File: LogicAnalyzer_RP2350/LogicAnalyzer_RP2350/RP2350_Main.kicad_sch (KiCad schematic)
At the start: 37 parts, among them J3 SM03B-SRSS-TB, SW1 SW_MEC_5G, SW2 SW_MEC_5G, U3 RP2350A, U4 W25Q128JVS, Y1 12Mhz

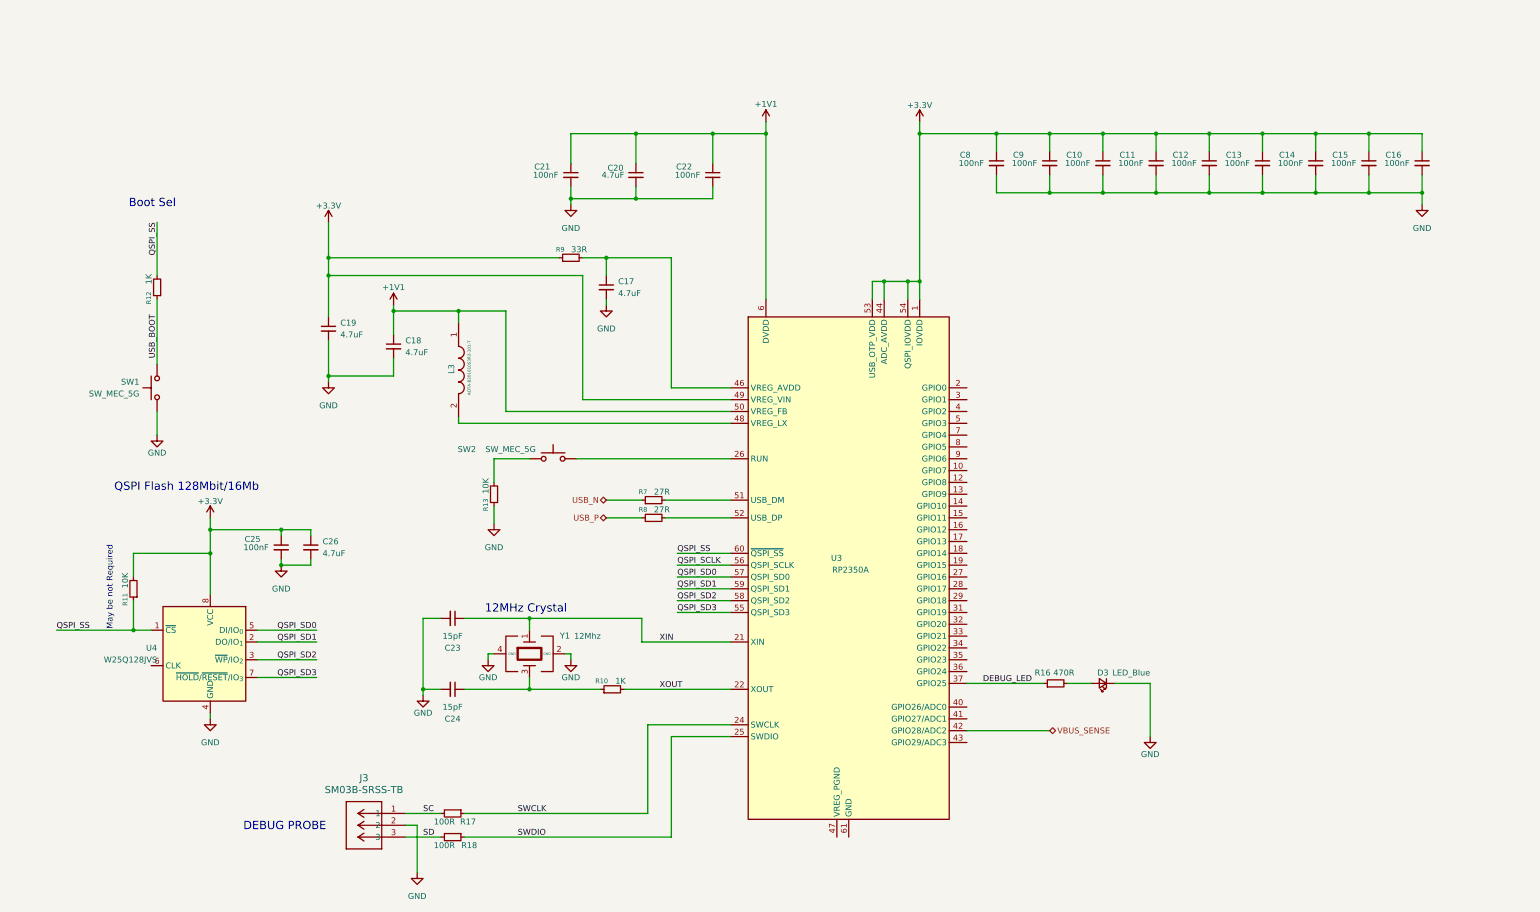
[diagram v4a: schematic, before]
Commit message: Added Buses for Logic Input Pins and Sheet for Shift Registers
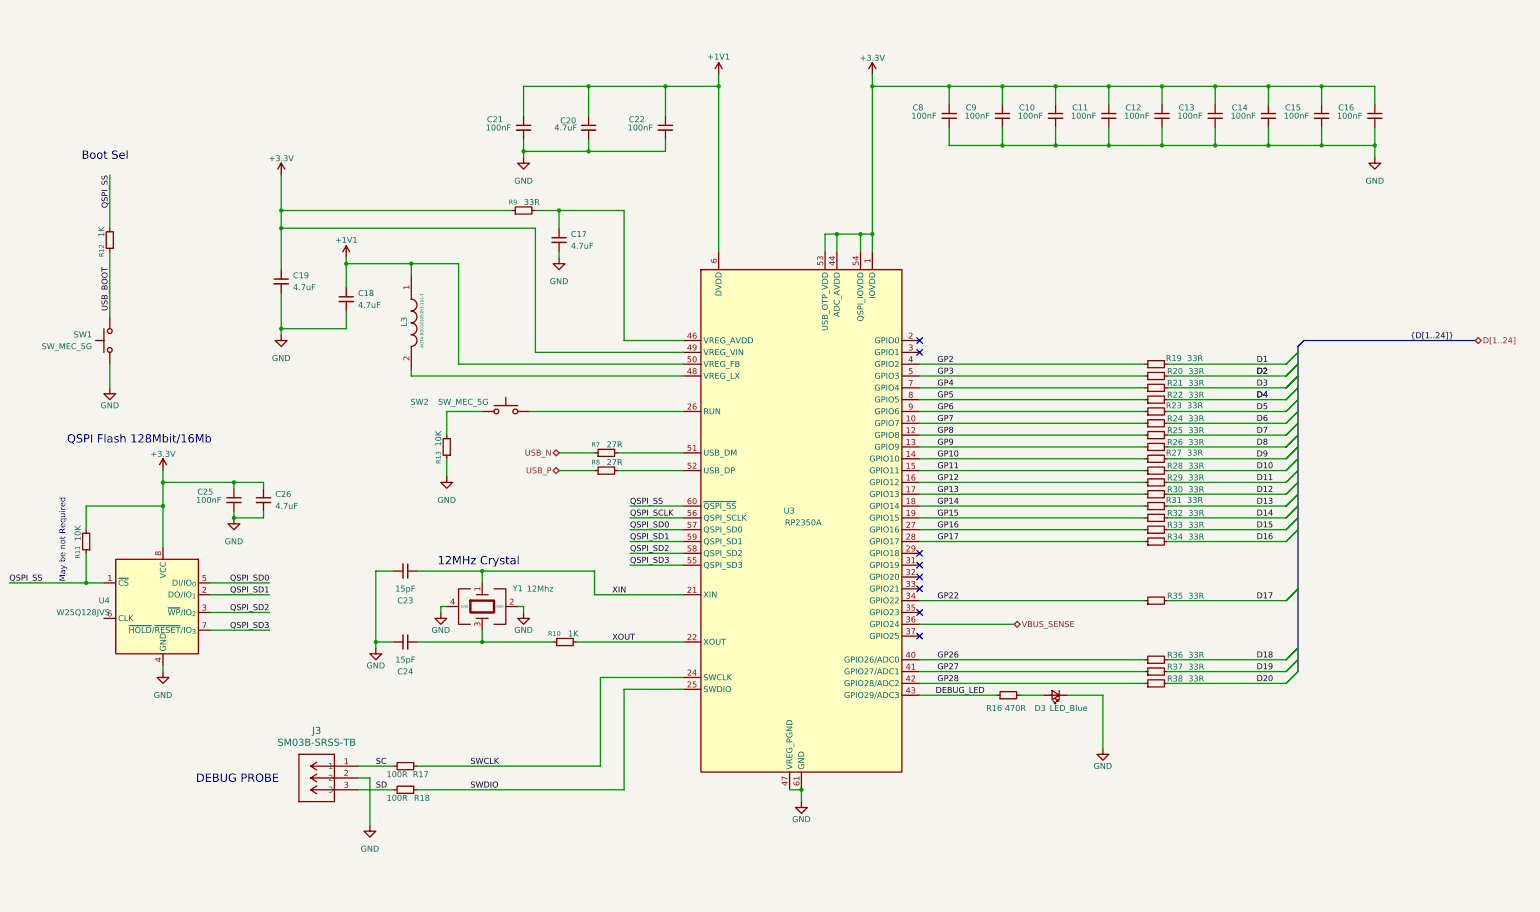
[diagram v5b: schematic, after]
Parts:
- added R19, R20, R21, R22, R23, R24, R25, R26, R27, R28, R29, R30, R31, R32, R33, R34, R35, R36, R37, R38: 33R, Resistor_SMD:R_0603_1608Metric_Pad0.98x0.95mm_HandSolder, symbol Device:R_Small
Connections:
- net DEBUG_LED: now also U3.43 (GPIO29/ADC3); no longer U3.37 (GPIO25)
- net GND: now also U3.47 (VREG_PGND), U3.61 (GND)
- net VBUS_SENSE: now also U3.36 (GPIO24); no longer U3.42 (GPIO28/ADC2)
- net GP7: now reaches U3.10 (GPIO7)
- net GP7: now also R24.1
- net GP8: now reaches U3.12 (GPIO8)
- net GP8: now also R25.1
- net GP9: now reaches U3.13 (GPIO9)
- net GP9: now also R26.1
- net GP10: now reaches U3.14 (GPIO10)
- net GP10: now also R27.1
- net GP11: now reaches U3.15 (GPIO11)
- net GP11: now also R28.1
- net GP12: now reaches U3.16 (GPIO12)
- net GP12: now also R29.1
- net GP13: now reaches U3.17 (GPIO13)
- net GP13: now also R30.1
- net GP14: now reaches U3.18 (GPIO14)
- net GP14: now also R31.1
- net GP15: now reaches U3.19 (GPIO15)
- net GP15: now also R32.1
- net GP16: now reaches U3.27 (GPIO16)
- net GP16: now also R33.1
- net GP17: now reaches U3.28 (GPIO17)
- net GP17: now also R34.1
- net GP22: now reaches U3.34 (GPIO22)
- net GP22: now also R35.1
- net GP2: now reaches U3.4 (GPIO2)
- net GP2: now also R19.1
- net GP26: now reaches U3.40 (GPIO26/ADC0)
- net GP26: now also R36.1
- net GP27: now reaches U3.41 (GPIO27/ADC1)
- net GP27: now also R37.1
- net GP3: now reaches U3.5 (GPIO3)
- net GP3: now also R20.1
- net GP4: now reaches U3.7 (GPIO4)
- net GP4: now also R21.1
- net GP5: now reaches U3.8 (GPIO5)
- net GP5: now also R22.1
- net GP6: now reaches U3.9 (GPIO6)
- net GP6: now also R23.1
- new net D1: R19.2
- new net D10: R28.2
- new net D11: R29.2
- new net D12: R30.2
- new net D13: R31.2
- new net D14: R32.2
- new net D15: R33.2
- new net D16: R34.2
- new net D17: R35.2
- new net D18: R36.2
- new net D19: R37.2
- new net D2: R20.2
- new net D20: R38.2
- new net D3: R21.2
- new net D4: R22.2
- new net D5: R23.2
- new net D6: R24.2
- new net D7: R25.2
- new net D8: R26.2
- new net D9: R27.2
- new net GP28: R38.1, U3.42 (GPIO28/ADC2)
- no-connect marks 0 -> 8
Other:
- moved on the sheet: C10, C11, C12, C13, C14, C15, C16, C17, C18, C19, C20, C21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

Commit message: Renaming
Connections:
- net DEBUG_LED renamed Debug_Led
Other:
- note added: "DEBUG Led"
- note added: "RESET"
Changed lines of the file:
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@@
+		)
+	)
+	(text "DEBUG Led"
+		(exclude_from_sim no)
+		(at 256.794 191.262 0)
+		(effects
+			(font
+				(size 1.778 1.778)
+				(color 0 0 255 1)
+			)
+		)
+	)
+	(text "RESET"
+		(exclude_from_sim no)
+		(at 118.872 130.556 90)
+		(effects
+			(font
+				(size 1.778 1.778)
+				(color 0 0 255 1)
+			)
 		)
 	)
@@
 		)
 	)
-	(label "DEBUG_LED"
+	(label "Debug_Led"
 		(at 242.57 184.15 180)
 		(effects
 			(font
 				(size 1.27 1.27)
-				(color 0 0 255 1)
+				(color 0 0 0 1)
 			)
 			(justify right bottom)

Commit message: Added EXT VREF, TRIG, ROTARY SWITCH, DAISY CHAIN CONNECTIONS etc
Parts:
- added R41: 33R, Resistor_SMD:R_0603_1608Metric_Pad0.98x0.95mm_HandSolder, symbol Device:R_Small
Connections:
- net at U3.2 (GPIO0): now also U3.3 (GPIO1), R41.1
- new net EXT_CHAIN: R41.2
- no-connect marks 8 -> 6
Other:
- moved on the sheet: R13, SW2
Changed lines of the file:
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@@
 	(text "RESET"
 		(exclude_from_sim no)
-		(at 118.872 130.556 90)
+		(at 107.442 130.556 90)
 		(effects
 			(font
@@
 	)
 	(junction
+		(at 229.87 107.95)
+		(diameter 0)
+		(color 0 0 0 0)
+	)
+	(junction
 		(at 292.1 66.04)
 		(diameter 0)
@@
 	)
 	(no_connect
-		(at 228.6 107.95)
-	)
-	(no_connect
 		(at 228.6 158.75)
 	)
@@
 		(at 228.6 171.45)
 	)
-	(no_connect
-		(at 228.6 110.49)
-	)
 	(bus_entry
 		(at 307.34 113.03)
@@
 	(wire
 		(pts
-			(xy 151.13 132.08) (xy 158.75 132.08)
+			(xy 139.7 132.08) (xy 158.75 132.08)
 		)
 		(stroke
@@
 	(wire
 		(pts
-			(xy 151.13 135.89) (xy 158.75 135.89)
+			(xy 139.7 135.89) (xy 158.75 135.89)
 		)
 		(stroke
@@
 	(wire
 		(pts
-			(xy 144.78 123.19) (xy 177.8 123.19)
+			(xy 133.35 123.19) (xy 177.8 123.19)
 		)
 		(stroke
@@
 	(wire
 		(pts
+			(xy 229.87 107.95) (xy 229.87 110.49)
+		)
+		(stroke
+			(width 0)
+			(type default)
+		)
+	)
+	(wire
+		(pts
 			(xy 228.6 148.59) (xy 276.86 148.59)
 		)
@@
 	(wire
 		(pts
+			(xy 229.87 107.95) (xy 245.11 107.95)
+		)
+		(stroke
+			(width 0)
+			(type default)
+		)
+	)
+	(wire
+		(pts
 			(xy 260.35 184.15) (xy 267.97 184.15)
 		)
@@
 	(wire
 		(pts
+			(xy 228.6 110.49) (xy 229.87 110.49)
+		)
+		(stroke
+			(width 0)
+			(type default)
+		)
+	)
+	(wire
+		(pts
 			(xy 158.75 162.56) (xy 158.75 157.48)
 		)
@@
 	(wire
 		(pts
+			(xy 250.19 107.95) (xy 265.43 107.95)
+		)
+		(stroke
+			(width 0)
+			(type default)
+		)
+	)
+	(wire
+		(pts
 			(xy 185.42 88.9) (xy 185.42 53.34)
 		)
@@
 	(wire
 		(pts
-			(xy 127 133.35) (xy 127 137.16)
+			(xy 228.6 107.95) (xy 229.87 107.95)
+		)
+		(stroke
+			(width 0)
+			(type default)
+		)
+	)
+	(wire
+		(pts
+			(xy 115.57 133.35) (xy 115.57 137.16)
 		)
 		(stroke
@@
 	(wire
 		(pts
-			(xy 127 123.19) (xy 134.62 123.19)
+			(xy 115.57 123.19) (xy 123.19 123.19)
 		)
 		(stroke
@@
 	(wire
 		(pts
-			(xy 127 128.27) (xy 127 123.19)
+			(xy 115.57 128.27) (xy 115.57 123.19)
 		)
 		(stroke
@@
 	(hierarchical_label "USB_P"
 		(shape bidirectional)
-		(at 151.13 135.89 180)
+		(at 139.7 135.89 180)
 		(effects
 			(font
@@
 	(hierarchical_label "USB_N"
 		(shape bidirectional)
-		(at 151.13 132.08 180)
+		(at 139.7 132.08 180)
 		(effects
 			(font
@@
 		)
 	)
+	(hierarchical_label "EXT_CHAIN"
+		(shape bidirectional)
+		(at 265.43 107.95 0)
+		(effects
+			(font
+				(size 1.27 1.27)
+			)
+			(justify left)
+		)
+	)
 	(symbol
 		(lib_id "Device:C_Small")
@@
 	(symbol
 		(lib_id "Switch:SW_MEC_5G")
-		(at 139.7 123.19 0)
+		(at 128.27 123.19 0)
 		(mirror y)
 		(unit 1)
@@
 		(dnp no)
 		(property "Reference" "SW2"
-			(at 121.158 121.158 0)
+			(at 109.728 121.158 0)
 			(show_name no)
 			(do_not_autoplace no)
@@
 		)
 		(property "Value" "SW_MEC_5G"
-			(at 130.556 121.158 0)
+			(at 119.126 121.158 0)
 			(show_name no)
 			(do_not_autoplace no)
@@
 		)
 		(property "Footprint" "SKRPABE010:SW4_SKRPABE010_ALPS"
-			(at 139.7 118.11 0)
+			(at 128.27 118.11 0)
 			(hide yes)
 			(show_name no)
@@
 		)
 		(property "Datasheet" "https://tech.alpsalpine.com/cms.media/product_spec_skrpabe010_en_c1c577738a.pdf"
-			(at 139.7 118.11 0)
+			(at 128.27 118.11 0)
 			(hide yes)
 			(show_name no)
@@
 		)
 		(property "Description" "Tactile Switch SPST-NO Top Actuated Surface Mount"
-			(at 139.7 123.19 0)
+			(at 128.27 123.19 0)
 			(hide yes)
 			(show_name no)
@@
 	(symbol
 		(lib_id "Device:R_Small")
-		(at 127 130.81 180)
+		(at 115.57 130.81 180)
 		(unit 1)
 		(body_style 1)
@@
 		(dnp no)
 		(property "Reference" "R13"
-			(at 125.222 133.096 90)
+			(at 113.792 133.096 90)
 			(show_name no)
 			(do_not_autoplace no)
@@
 		)
 		(property "Value" "10K"
-			(at 125.222 129.032 90)
+			(at 113.792 129.032 90)
 			(show_name no)
 			(do_not_autoplace no)
@@
 		)
 		(property "Footprint" "Resistor_SMD:R_0603_1608Metric_Pad0.98x0.95mm_HandSolder"
-			(at 127 130.81 0)
+			(at 115.57 130.81 0)
 			(hide yes)
 			(show_name no)
@@
 		)
 		(property "Datasheet" ""
-			(at 127 130.81 0)
+			(at 115.57 130.81 0)
 			(hide yes)
 			(show_name no)
@@
 		)
 		(property "Description" "Resistor, small symbol"
-			(at 127 130.81 0)
+			(at 115.57 130.81 0)
 			(hide yes)
 			(show_name no)
@@
 	)
 	(symbol
+		(lib_id "Device:R_Small")
+		(at 247.65 107.95 90)
+		(unit 1)
+		(body_style 1)
+		(exclude_from_sim no)
+		(in_bom yes)
+		(on_board yes)
+		(in_pos_files yes)
+		(dnp no)
+		(property "Reference" "R41"
+			(at 251.46 106.68 90)
+			(show_name no)
+			(do_not_autoplace no)
+			(effects
+				(font
+					(size 1.27 1.27)
+				)
+			)
+		)
+		(property "Value" "33R"
+			(at 256.032 106.68 90)
+			(show_name no)
+			(do_not_autoplace no)
+			(effects
+				(font
+					(size 1.27 1.27)
+				)
+			)
+		)
+		(property "Footprint" "Resistor_SMD:R_0603_1608Metric_Pad0.98x0.95mm_HandSolder"
+			(at 247.65 107.95 0)
+			(hide yes)
+			(show_name no)
+			(do_not_autoplace no)
+			(effects
+				(font
+					(size 1.27 1.27)
+				)
+			)
+		)
+		(property "Datasheet" ""
+			(at 247.65 107.95 0)
+			(hide yes)
+			(show_name no)
+			(do_not_autoplace no)
+			(effects
+				(font
+					(size 1.27 1.27)
+				)
+			)
+		)
+		(property "Description" "Resistor, small symbol"
+			(at 247.65 107.95 0)
+			(hide yes)
+			(show_name no)
+			(do_not_autoplace no)
+			(effects
+				(font
+					(size 1.27 1.27)
+				)
+			)
+		)
+		(pin "2"
+		)
+		(pin "1"
+		)
+		(instances
+			(project "LogicAnalyzer_RP2350"
+				(path "/d75f24d0-99d8-459e-8e7b-473191ec3959/08028c02-6110-45a5-bc16-9b1936572182"
+					(reference "R41")
+					(unit 1)
+				)
+			)
+		)
+	)
+	(symbol
 		(lib_id "Memory_Flash:W25Q128JVS")
 		(at 66.04 165.1 0)
@@
 	(symbol
 		(lib_id "power:GND")
-		(at 127 137.16 0)
+		(at 115.57 137.16 0)
 		(unit 1)
 		(body_style 1)
@@
 		(fields_autoplaced yes)
 		(property "Reference" "#PWR027"
-			(at 127 143.51 0)
+			(at 115.57 143.51 0)
 			(hide yes)
 			(show_name no)
@@
 		)
 		(property "Value" "GND"
-			(at 127 142.24 0)
+			(at 115.57 142.24 0)
 			(show_name no)
 			(do_not_autoplace no)
@@
 		)
 		(property "Footprint" ""
-			(at 127 137.16 0)
+			(at 115.57 137.16 0)
 			(hide yes)
 			(show_name no)
@@
 		)
 		(property "Datasheet" ""
-			(at 127 137.16 0)
+			(at 115.57 137.16 0)
 			(hide yes)
 			(show_name no)
@@
 		)
 		(property "Description" "Power symbol creates a global label with name \"GND\" , ground"
-			(at 127 137.16 0)
+			(at 115.57 137.16 0)
 			(hide yes)
 			(show_name no)

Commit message: SOME AESTHETIC SCHEMATIC CHANGES
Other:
- note added: "12MHZ CRYSTAL"
- note added: "BOOT SEL"
- note added: "QSPI FLASH 125Mbit"
- note removed: "12MHz Crystal"
- note removed: "Boot Sel"
- note removed: "QSPI Flash 128Mbit/16Mb"
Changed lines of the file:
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@@
 	(generator_version "10.0")
 	(paper "A3")
-	(text "12MHz Crystal"
+	(text "12MHZ CRYSTAL"
 		(exclude_from_sim no)
 		(at 133.858 155.448 0)
@@
 		)
 	)
-	(text "Boot Sel"
+	(text "BOOT SEL"
 		(exclude_from_sim no)
 		(at 53.594 68.326 0)
@@
 		)
 	)
-	(text "QSPI Flash 128Mbit/16Mb\n"
+	(text "QSPI FLASH 125Mbit"
 		(exclude_from_sim no)
 		(at 60.96 129.286 0)
